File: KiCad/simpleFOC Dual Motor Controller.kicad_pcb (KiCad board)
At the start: 4 copper layers, 50 x 50 mm, 95 parts, among them CN201 MR60-F, CN202 MR60-F, J101 Conn_01x04, Q101 AGM6014AP, Q102 AGM6014AP, Q103 AGM6014AP, Q104 AGM6014AP, Q105 AGM6014AP, Q106 AGM6014AP, Q301 AGM6014AP, Q303 AGM6014AP, Q401 AGM6014AP, Q403 AGM6014AP, Q501 AGM6014AP, Q503 AGM6014AP, SW101 TS-1088-AR02016, U101 STM32F103C8Tx, U102 XT60H-M, U201 DRV8323HRTAT, U202 DRV8323HRTAT

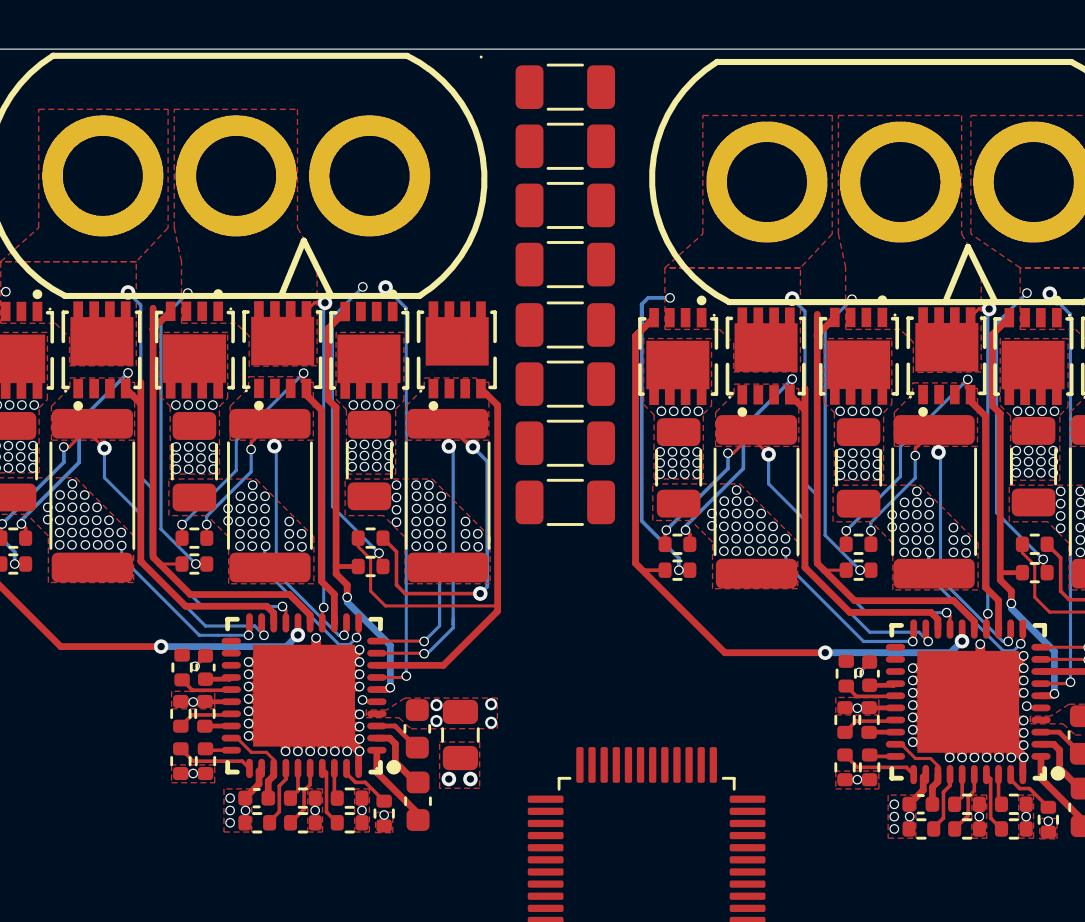
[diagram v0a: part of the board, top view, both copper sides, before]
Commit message: updated configuration for new mosfets
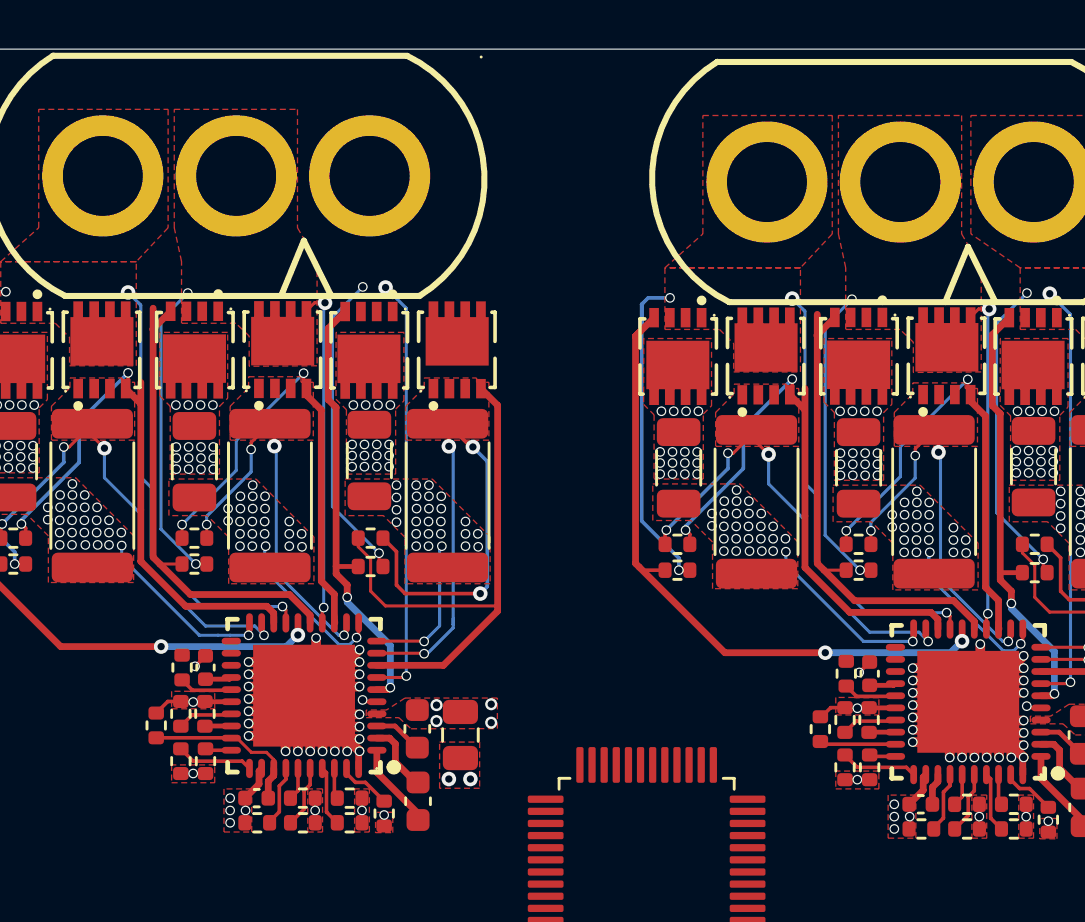
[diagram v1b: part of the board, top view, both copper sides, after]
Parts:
- removed the C401 at (124.9, 31.4)
- removed the C401 at (124.9, 29.0)
- removed the C401 at (124.9, 38.8)
- removed the C401 at (124.9, 43.7)
- removed the C401 at (124.9, 26.6)
- removed the C401 at (124.9, 33.9)
- removed the C401 at (124.9, 41.2)
- removed the C401 at (124.9, 36.4)
- added R223: 47k, Resistor_SMD:R_0402_1005Metric, F.Cu at (135.4, 53.0)
- added R601: 47k, Resistor_SMD:R_0402_1005Metric, F.Cu at (108.1, 52.9)
- R201, R213: value 75k -> 18k
- Rsns101, Rsns102, Rsns103, Rsns301, Rsns401, Rsns501: value 0.001 -> 0.002
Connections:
- R211 pad 1: /Motor Driver 1/~{FAULT} -> /FAULT1
- R222 pad 1: /Motor Driver 2/~{FAULT} -> /FAULT2
- U101 pad 2: unconnected-(U101-PC13-Pad2) -> /GAIN1
- U101 pad 4: unconnected-(U101-PC15-Pad4) -> /GAIN2
- U201 pad 25: /Motor Driver 1/~{FAULT} -> /FAULT1
- U201 pad 29: /Motor Driver 1/DVDD -> /GAIN1
- U202 pad 25: /Motor Driver 2/~{FAULT} -> /FAULT2
- U202 pad 29: /Motor Driver 2/DVDD -> /GAIN2
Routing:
- net /GAIN2: track 0.00 -> 3.10 mm
- net /GAIN1: track 0.00 -> 3.09 mm
- net GND: track 146.8 -> 149.1 mm
- net /Motor Driver 1/DVDD: track 3.56 -> 1.32 mm
- net /Motor Driver 2/~{FAULT}: track 2.22 -> 0.00 mm
- net /FAULT2: track 0.00 -> 2.22 mm
- net /Motor Driver 1/~{FAULT}: track 2.22 -> 0.00 mm
- net /FAULT1: track 0.00 -> 2.22 mm

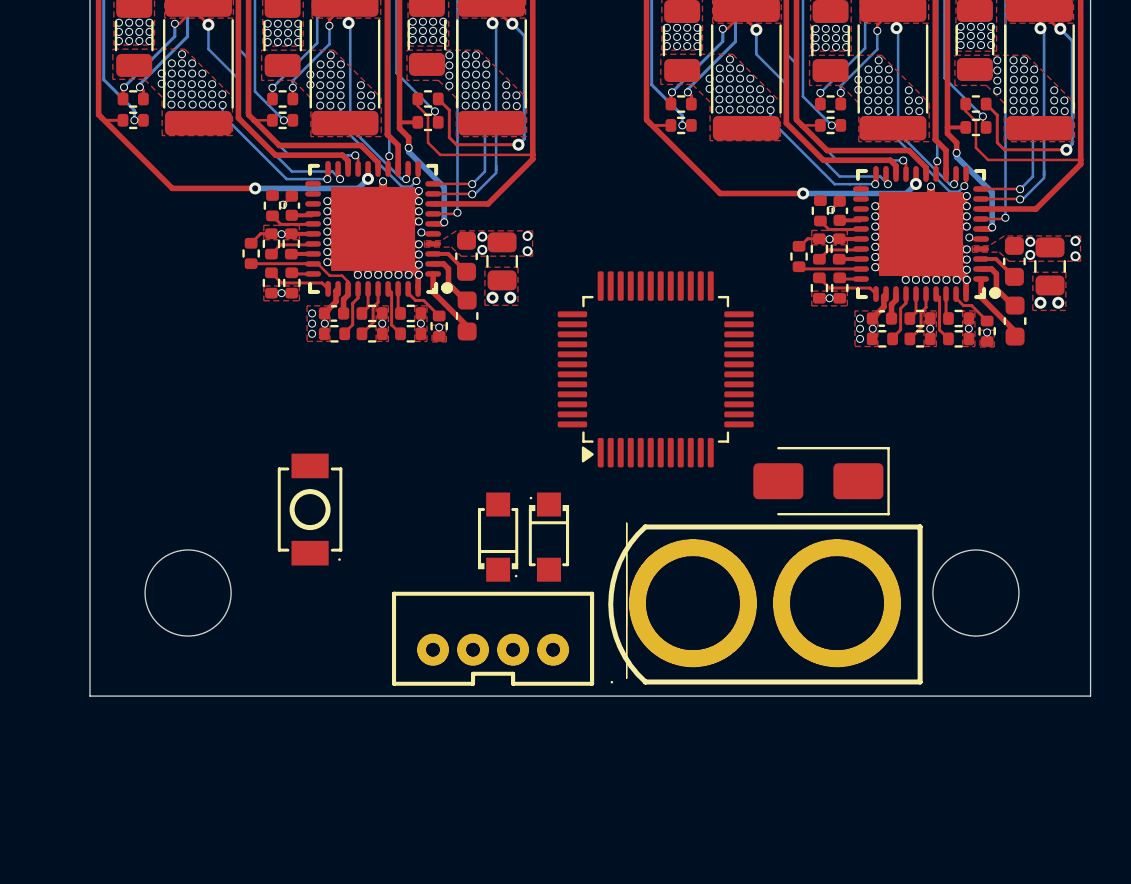
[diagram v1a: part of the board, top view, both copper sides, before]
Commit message: swapped CPU for ESP32
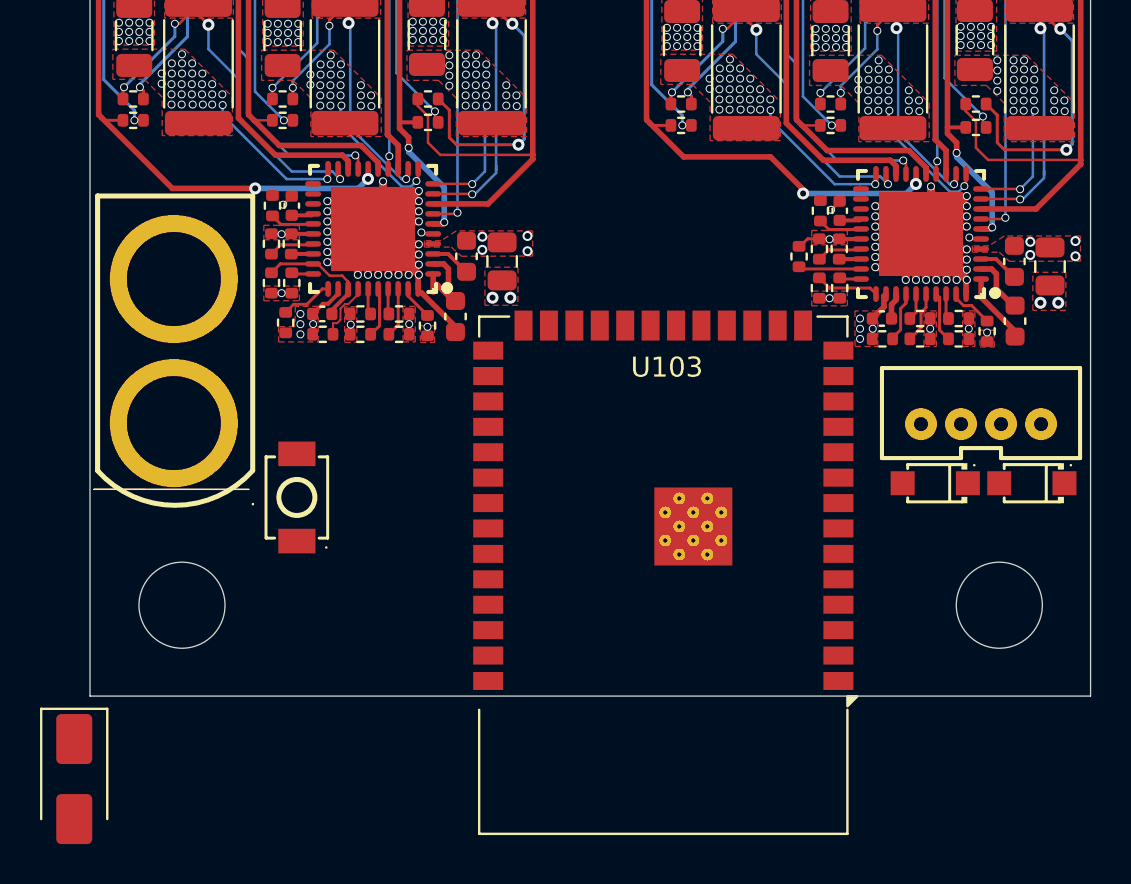
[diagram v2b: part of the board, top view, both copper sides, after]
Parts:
- removed U101: STM32F103C8Tx, Package_QFP:LQFP-48_7x7mm_P0.5mm
- added U103: ESP32-S3-WROOM-1, RF_Module:ESP32-S3-WROOM-1, F.Cu at (128.6, 69.0)
- moved D101 40.1 mm to (99.2, 79.1), turned to -90 degrees
- moved U102 32.1 mm to (104.2, 57.8), turned to 90 degrees
- moved J101 26.9 mm to (144.5, 60.9)
- moved D103 24.3 mm to (147.1, 64.4), turned to 180 degrees
- moved D104 22.0 mm to (142.2, 64.4), turned to 180 degrees
- moved R221 2.10 mm to (109.8, 56.3)
- moved R601 1.79 mm to (109.1, 54.4), turned to -90 degrees
- moved H101 1.32 mm to (145.4, 70.5)
- moved R218 1.19 mm to (115.4, 56.9)
- moved R217 1.15 mm to (115.4, 55.9)
- moved SW101 0.90 mm to (110.3, 65.1)
- moved H102 0.68 mm to (104.6, 70.5)
- moved R214 0.58 mm to (111.6, 56.9)
- moved R219 0.58 mm to (116.9, 56.5)
- moved C208 0.58 mm to (118.3, 56.0)
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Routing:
- net /CHC2: track 1.27 -> 2.46 mm
- net /CHBn2: track 2.50 -> 1.43 mm
- net /GAIN2: track 3.10 -> 2.27 mm
- net GND: track 149.1 -> 148.4 mm
- net /Motor Driver 2/DVDD: track 3.56 -> 4.12 mm
- net /CAL2: track 3.16 -> 2.60 mm
- net /CHCn2: track 2.23 -> 1.73 mm

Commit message: started laying out
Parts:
- removed D103: DSK26_C7502712, easyeda2kicad:SOD-123FL_L2.7-W1.8-LS3.8-RD
- removed H101, H102: MountingHole, MountingHole:MountingHole_4.3mm_M4
- removed R207, R208, R217, R218, R219: 100k, Resistor_SMD:R_0402_1005Metric
- added C103: 100n, Capacitor_SMD:C_01005_0402Metric, F.Cu at (89.8, 49.1)
- added C104: 22u, Capacitor_SMD:C_1206_3216Metric, F.Cu at (85.8, 50.0)
- added C105: 1u, Capacitor_SMD:C_01005_0402Metric, F.Cu at (94.1, 50.9)
- added C111: C_Small, Capacitor_SMD:C_01005_0402Metric, F.Cu at (89.8, 50.8)
- added D102: B16WS_C7420327, easyeda2kicad:SOD-323_L1.7-W1.3-LS2.5-FD, F.Cu at (84.9, 52.9)
- added D105: H5VL06B, easyeda2kicad:X3-DFN0603-2_L0.6-W0.3-BI, F.Cu at (90.8, 55.7)
- added D106: H5VL06B, easyeda2kicad:X3-DFN0603-2_L0.6-W0.3-BI, F.Cu at (90.8, 57.3)
- added D107: B16WS_C7420327, easyeda2kicad:SOD-323_L1.7-W1.3-LS2.5-FD, F.Cu at (84.9, 55.5)
- added J102: USB_C_Receptacle_USB2.0_14P, Connector_USB:USB_C_Receptacle_HCTL_HC-TYPE-C-16P-01A, F.Cu at (102.4, 53.9)
- added R107: 5.1k, PCM_SparkFun-Resistor:R_0402_1005Metric, F.Cu at (88.3, 55.8)
- added R108: 5.1k, Resistor_THT:R_Axial_DIN0204_L3.6mm_D1.6mm_P1.90mm_Vertical, F.Cu at (88.5, 53.2)
- added R108: 5.1k, PCM_SparkFun-Resistor:R_0402_1005Metric, F.Cu at (87.3, 45.5)
- added R109: 10k, PCM_SparkFun-Resistor:R_0402_1005Metric, F.Cu at (88.3, 57.8)
- added R224: 47k, Resistor_SMD:R_0402_1005Metric, F.Cu at (136.5, 49.7)
- added R602: 47k, Resistor_SMD:R_0402_1005Metric, F.Cu at (109.1, 49.4)
- added R603: 100k, Resistor_SMD:R_0402_1005Metric, F.Cu at (114.5, 55.8)
- added U101: XC6206P332MR, easyeda2kicad:SOT-23-3_L2.9-W1.6-P1.90-LS2.8-BR, F.Cu at (95.2, 48.0)
- moved D101 59.0 mm to (156.1, 63.6), turned to 90 degrees
- moved U102 42.5 mm to (145.8, 66.0), turned to -90 degrees
- moved D104 41.0 mm to (101.3, 62.0), turned to -90 degrees
- moved J101 39.8 mm to (104.9, 64.5), turned to 90 degrees
- moved SW101 22.8 mm to (129.2, 52.4), turned to 0 degrees
- moved R216 2.51 mm to (115.9, 56.2), turned to -90 degrees
- moved R221 2.10 mm to (109.1, 54.4)
- moved R205 1.94 mm to (143.3, 56.5), turned to -90 degrees
- moved R206 1.93 mm to (141.8, 56.0)
- moved R601 1.87 mm to (108.1, 52.8), turned to 90 degrees
- moved R215 1.30 mm to (114.5, 56.8), turned to 0 degrees
- moved C205 1.07 mm to (137.5, 49.7)
- moved C209 1.07 mm to (110.1, 49.4)
- moved R204 0.98 mm to (141.8, 57.0)
- moved R214 0.95 mm to (112.6, 56.8)
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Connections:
- R204 pad 1: /CHAn1 -> /CHB1
- R205 pad 1: /CHB1 -> /CHC1
- R206 pad 1: /CHBn1 -> /Motor Driver 1/~{HI-Z}
- R215 pad 1: /CHAn2 -> /CHB2
- R216 pad 1: /CHB2 -> /CHC2
- U103 pad 1: Net-(U103-GND-Pad1) -> GND
- U103 pad 10: unconnected-(U103-IO17-Pad10) -> /snsB2
- U103 pad 11: unconnected-(U103-IO18-Pad11) -> /snsC2
- U103 pad 12: unconnected-(U103-IO8-Pad12) -> /EN2
- U103 pad 13: unconnected-(U103-USB_D--Pad13) -> /D-
- U103 pad 14: unconnected-(U103-USB_D+-Pad14) -> /D+
- U103 pad 17: unconnected-(U103-IO9-Pad17) -> /sns_cs1
- U103 pad 18: unconnected-(U103-IO10-Pad18) -> /FAULT2
- U103 pad 19: unconnected-(U103-IO11-Pad19) -> /GAIN2
- U103 pad 2: unconnected-(U103-3V3-Pad2) -> +3.3V
- U103 pad 20: unconnected-(U103-IO12-Pad20) -> /ctrl_scl
- U103 pad 21: unconnected-(U103-IO13-Pad21) -> /ctrl_sda
- U103 pad 22: unconnected-(U103-IO14-Pad22) -> /sns_sck
- U103 pad 23: unconnected-(U103-IO21-Pad23) -> /sns_cs2
- U103 pad 24: unconnected-(U103-IO47-Pad24) -> /sns_miso
- U103 pad 25: unconnected-(U103-IO48-Pad25) -> /sns_mosi
- U103 pad 28: unconnected-(U103-IO35-Pad28) -> /FAULT1
- U103 pad 29: unconnected-(U103-IO36-Pad29) -> /GAIN1
- U103 pad 3: unconnected-(U103-EN-Pad3) -> /~{rst}
- U103 pad 31: unconnected-(U103-IO38-Pad31) -> /CAL1
- U103 pad 32: unconnected-(U103-IO39-Pad32) -> /EN1
- U103 pad 33: unconnected-(U103-IO40-Pad33) -> /CHC1
- U103 pad 34: unconnected-(U103-IO41-Pad34) -> /CHB1
- U103 pad 35: unconnected-(U103-IO42-Pad35) -> /CHA1
- U103 pad 38: unconnected-(U103-IO2-Pad38) -> /snsB1
- U103 pad 39: unconnected-(U103-IO1-Pad39) -> /snsA1
- U103 pad 4: unconnected-(U103-IO4-Pad4) -> /snsC1
- U103 pad 40: Net-(U103-GND-Pad1) -> GND
- U103 pad 41: Net-(U103-GND-Pad1) -> GND
- U103 pad 5: unconnected-(U103-IO5-Pad5) -> /CHA2
- U103 pad 6: unconnected-(U103-IO6-Pad6) -> /CHB2
- U103 pad 7: unconnected-(U103-IO7-Pad7) -> /CHC2
- U103 pad 8: unconnected-(U103-IO15-Pad8) -> /CAL2
- U103 pad 9: unconnected-(U103-IO16-Pad9) -> /snsA2
- U201 pad 26: GND -> Net-(U201-MODE)
- U201 pad 35: /CHAn1 -> /Motor Driver 1/~{HI-Z}
- U201 pad 37: /CHBn1 -> /Motor Driver 1/~{HI-Z}
- U201 pad 39: /CHCn1 -> /Motor Driver 1/~{HI-Z}
- U202 pad 26: GND -> Net-(U202-MODE)
- U202 pad 35: /CHAn2 -> /~{HI-Z2}
- U202 pad 37: /CHBn2 -> /~{HI-Z2}
- U202 pad 39: /CHCn2 -> /~{HI-Z2}
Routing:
- net /Motor Driver 2/Pole 1/GL: track 23.2 -> 40.5 mm
- net GND: track 148.4 -> 135.2 mm, vias 220 -> 206
- net /Motor Driver 1/~{HI-Z}: track 0.00 -> 5.02 mm
- net /~{HI-Z2}: track 0.00 -> 5.02 mm
- net Net-(D104-K): track 0.00 -> 4.56 mm
- net Net-(U201-MODE): track 0.00 -> 3.29 mm
- net Net-(U202-MODE): track 0.00 -> 3.29 mm
- net /Motor Driver 2/DVDD: track 4.12 -> 1.18 mm
- net /CHBn1: track 2.50 -> 0.00 mm
- net /CHCn1: track 2.23 -> 0.00 mm
- net /CHCn2: track 1.73 -> 0.00 mm
- net Net-(U202-CPL): track 3.58 -> 1.91 mm
- net Net-(U201-CPL): track 3.58 -> 1.91 mm
- net /CHBn2: track 1.43 -> 0.00 mm
- net /CHAn1: track 1.35 -> 0.00 mm
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- added copper zone on F.Cu, net /Motor Driver 2/Pole 1/PoleOut

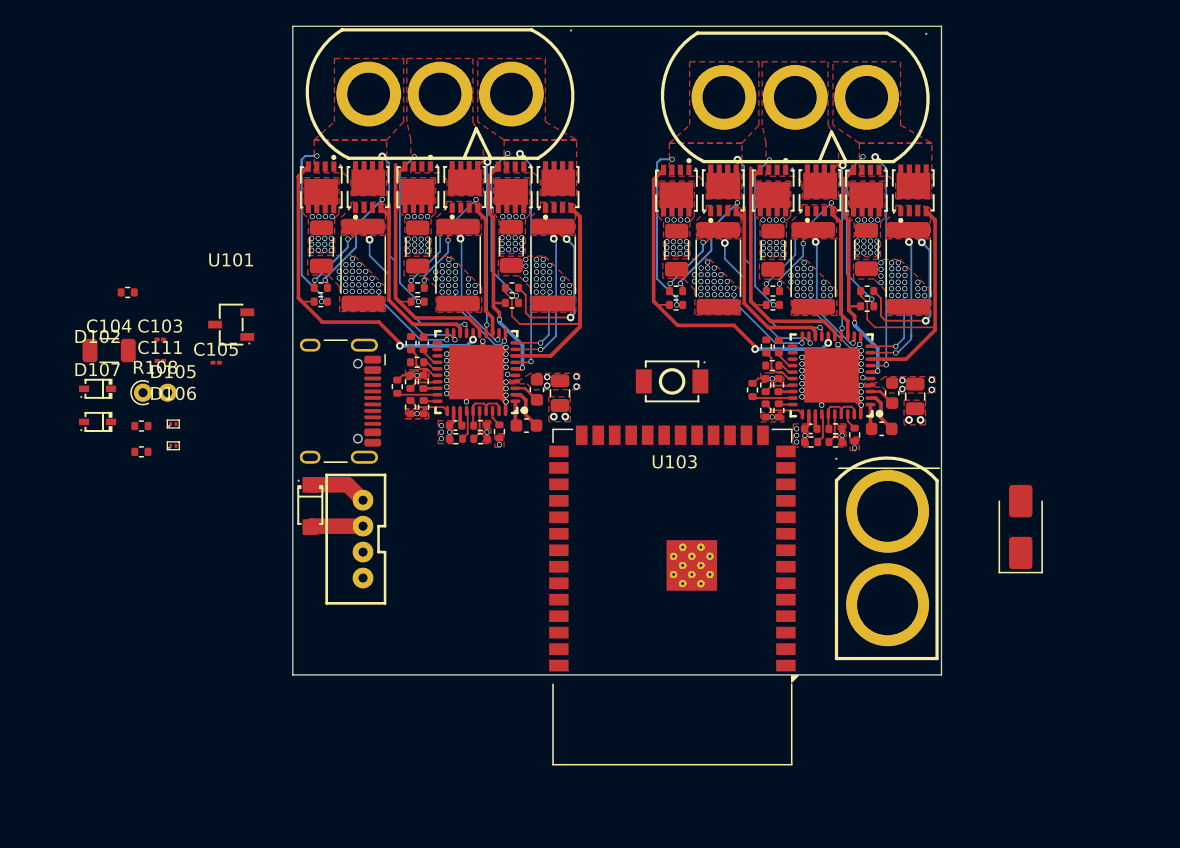
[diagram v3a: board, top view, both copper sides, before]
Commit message: added hall connectors
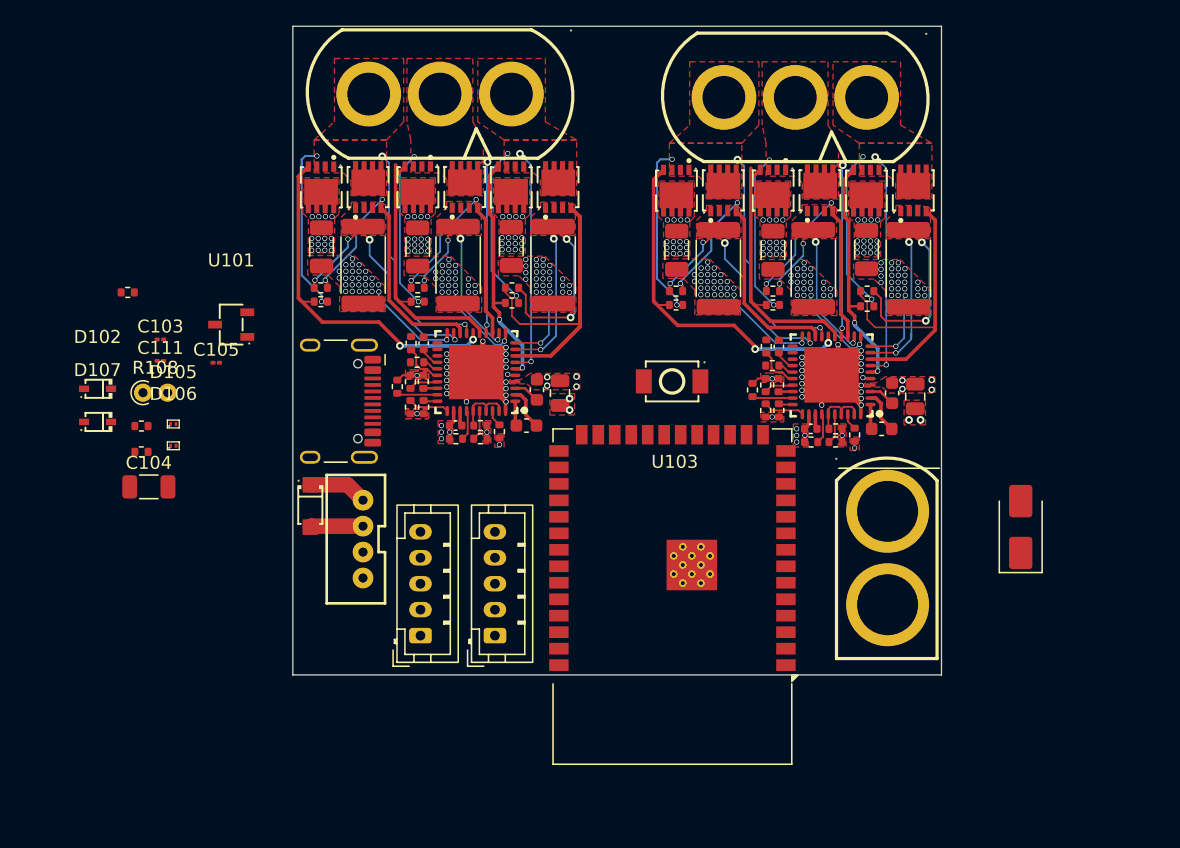
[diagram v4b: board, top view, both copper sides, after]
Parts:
- added J103: Conn_01x05_2.0mm, Connector_JST:JST_PH_B5B-PH-K_1x05_P2.00mm_Vertical, F.Cu at (109.8, 72.0)
- added J105: Conn_01x05_2.0mm, Connector_JST:JST_PH_B5B-PH-K_1x05_P2.00mm_Vertical, F.Cu at (115.6, 72.0)
- moved C104 10.9 mm to (88.9, 60.5)
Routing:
- net /Motor Driver 2/Pole 3/GL: track 24.5 -> 23.6 mm
- net /Motor Driver 1/Pole 3/GL: track 24.5 -> 23.6 mm
